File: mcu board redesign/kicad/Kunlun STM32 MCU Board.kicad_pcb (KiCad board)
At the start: 2 copper layers, 40 x 40 mm, 33 parts, among them J1 0532610671, J2 10129383-908001ALF, J3 USB4105-GF-A, J4 5002, J5 5002, J6 5002, J7 5002, J8 5001, J9 5001, SW1 KMR231NG ULC LFS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

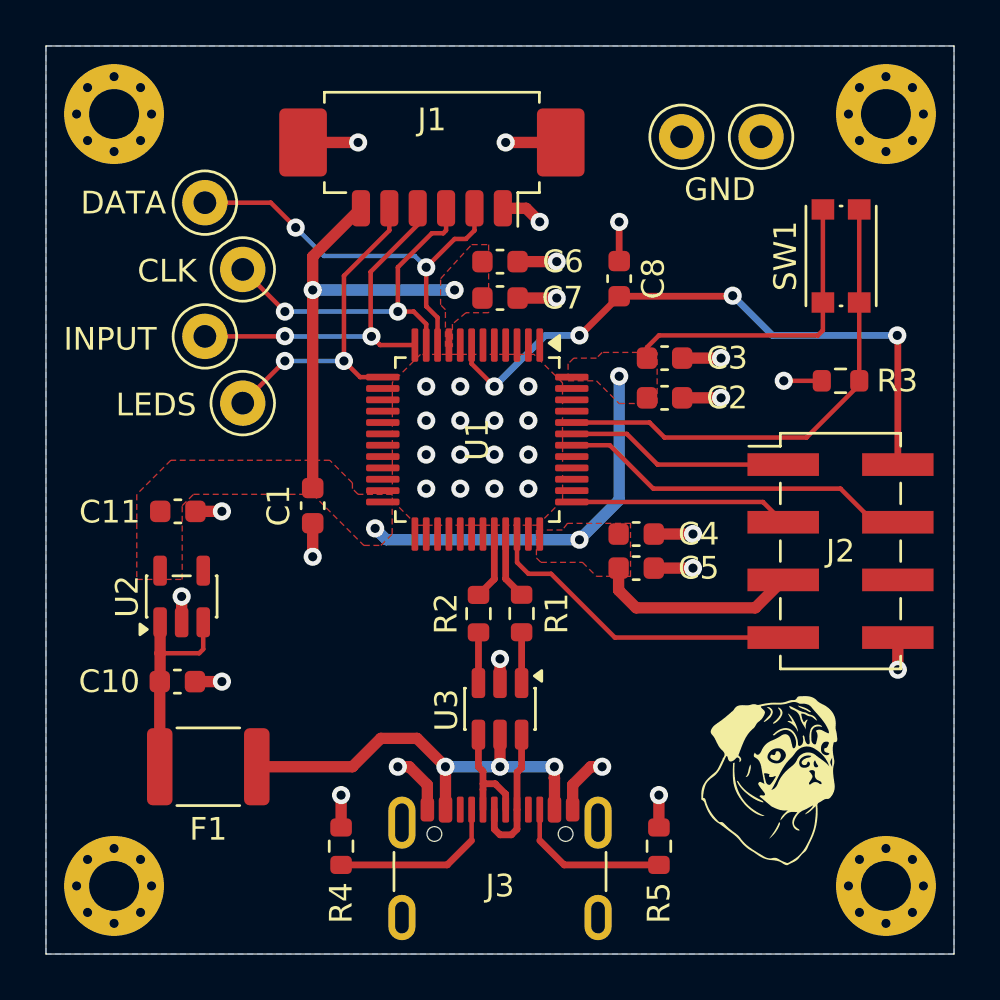
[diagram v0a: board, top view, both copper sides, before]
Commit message: Lots of updates
Add ESD protection R6/C9
Layout changes for bypass caps
Layout changes to pass all JLC DFM checks
Fill out J2 and optimize routing
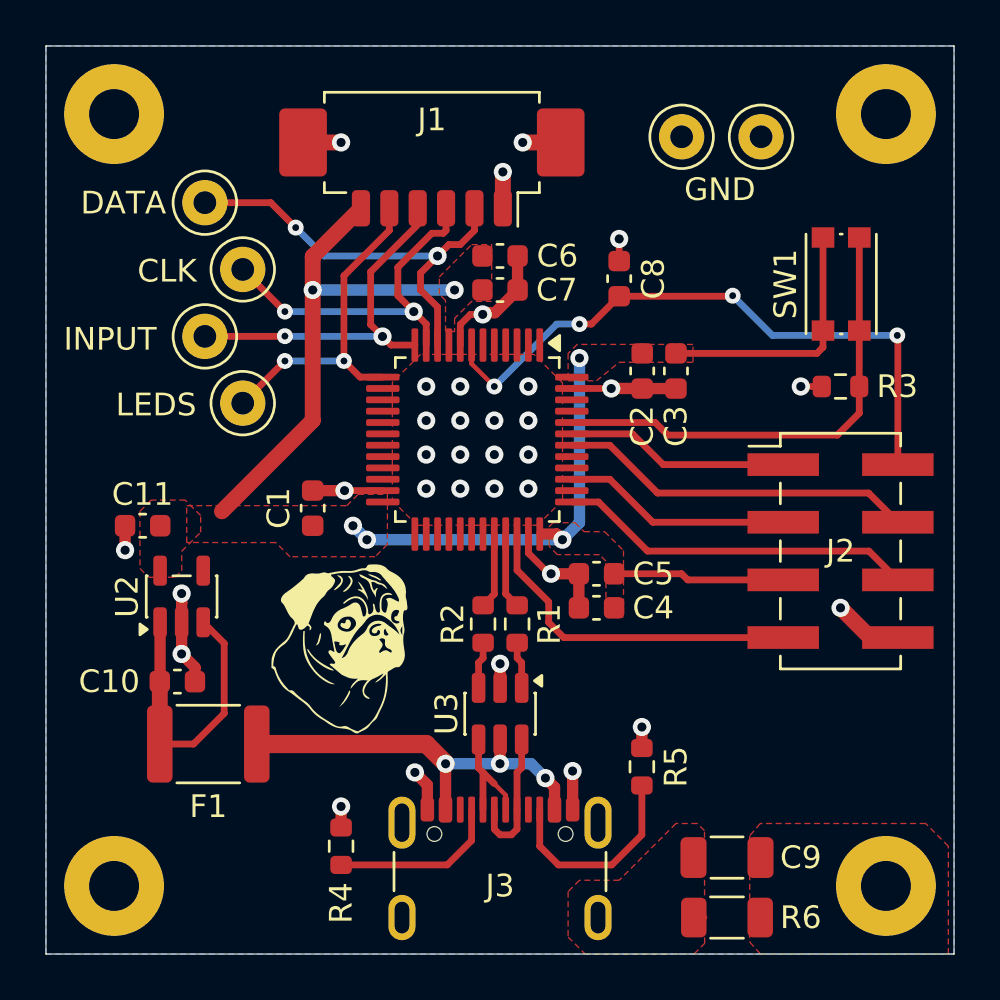
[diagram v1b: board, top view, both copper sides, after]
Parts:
- added C9: 1nF, Capacitor_SMD:C_1206_3216Metric, F.Cu at (158.2, 120.5)
- added R6: 1M, Resistor_SMD:R_1206_3216Metric, F.Cu at (158.2, 123.1)
- H1, H2, H3, H4: footprint MountingHole:MountingHole_2.2mm_M2_Pad_Via -> MountingHole:MountingHole_2.2mm_M2_Pad
- moved H1 48.1 mm to (165.2, 121.8)
- moved H2 48.1 mm to (131.2, 121.8)
- moved H3 34.0 mm to (131.2, 87.8)
- moved H4 34.0 mm to (165.2, 87.8)
- moved C4 3.69 mm to (152.5, 109.5), turned to 180 degrees
- moved R5 3.58 mm to (154.5, 116.5)
- moved C5 1.77 mm to (152.5, 108.0), turned to 180 degrees
- moved C11 1.67 mm to (132.5, 105.9), turned to 180 degrees
- moved C2 1.54 mm to (154.5, 99.1), turned to -90 degrees
- moved SW1 1.24 mm to (163.3, 95.2)
- moved F1 1.00 mm to (135.4, 115.5)
- moved C3 0.76 mm to (156.0, 99.1), turned to -90 degrees
- moved R1 0.50 mm to (149.0, 110.2)
- moved R2 0.50 mm to (147.5, 110.2)
- moved C7 0.35 mm to (148.2, 95.5)
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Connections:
- H1 pad 1: GND -> Net-(C9-Pad1)
- H2 pad 1: GND -> unconnected-(H2-Pad1)
- H3 pad 1: GND -> unconnected-(H3-Pad1)
- H4 pad 1: GND -> unconnected-(H4-Pad1)
- J2 pad 3: /SWCLK -> /DEBUG_GPIO
- J2 pad 6: unconnected-(J2-Pin_6-Pad6) -> /SWCLK
- R1 pad 1: Net-(R1-Pad1) -> /USB_D+
- R1 pad 2: /USB_D+ -> Net-(U1-PA12)
- R2 pad 1: Net-(R2-Pad1) -> /USB_D-
- R2 pad 2: /USB_D- -> Net-(U1-PA11)
- U1 pad 32: /USB_D- -> Net-(U1-PA11)
- U1 pad 33: /USB_D+ -> Net-(U1-PA12)
- U1 pad 39: unconnected-(U1-PB3-Pad39) -> /DEBUG_GPIO
- U3 pad 1: Net-(R1-Pad1) -> /USB_D+
- U3 pad 3: Net-(R2-Pad1) -> /USB_D-
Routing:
- net /DEBUG_GPIO: track 0.00 -> 10.1 mm
- net /SWCLK: track 9.68 -> 17.0 mm
- net +5V: track 9.53 -> 13.2 mm
- net GND: track 36.2 -> 39.6 mm, vias 36 -> 33
- net Net-(U1-PA12): track 0.00 -> 3.35 mm
- net Net-(U1-PA11): track 0.00 -> 3.34 mm
- net Net-(R1-Pad1): track 2.24 -> 0.00 mm
- net Net-(R2-Pad1): track 2.24 -> 0.00 mm
- net Net-(J3-CC2): track 7.06 -> 9.18 mm
- net VBUS: track 19.3 -> 17.9 mm
- net unconnected-(J2-Pin_6-Pad6): track 1.25 -> 0.00 mm
- net /USART1_TX: track 15.8 -> 16.8 mm
- net /USB_D-: track 2.97 -> 2.07 mm
- net /USB_D+: track 2.97 -> 2.07 mm
- net /SWDIO: track 14.3 -> 15.1 mm
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- added copper zone on F.Cu, net Net-(C9-Pad1)
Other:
- board text added: "J2 1-UART1_RX 2-NRST 3-PB3 4-UART1_TX 5-VDD (3.3V) 6-SWCLK 7-SWDIO 8-GND"
- board text removed: "J2 1-UART1_RX 2-NRST 3-SWCLK 4-UART1_TX 5-VDD (3.3V) 6- 7-SWDIO 8-GND"

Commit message: Mostly layout updates
Add VBUS decoupling cap.
Rearrange traces for less ground plane chops and fewer vias.
Move some components around for trace optimization (boot switch, etc)
Tweak the decoupling caps
Remove pads from 3 mounting holes to avoid potential chassis ground loops
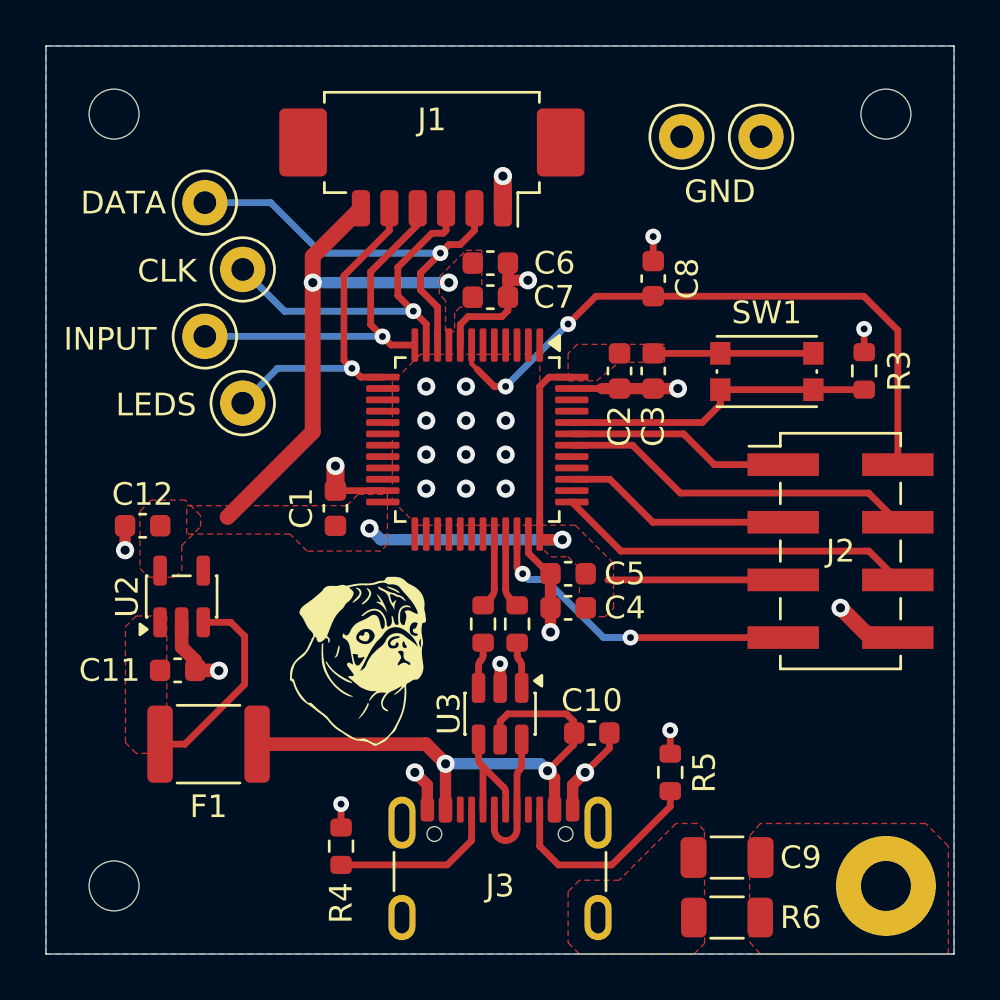
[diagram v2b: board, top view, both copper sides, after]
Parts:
- removed H2, H3, H4: MountingHole_Pad, MountingHole:MountingHole_2.2mm_M2_Pad
- added C10: 1uF, Capacitor_SMD:C_0603_1608Metric, F.Cu at (152.3, 115.0)
- added REF**: MountingHole_2.2mm_M2, MountingHole:MountingHole_2.2mm_M2, F.Cu at (131.2, 121.8)
- added REF**: MountingHole_2.2mm_M2, MountingHole:MountingHole_2.2mm_M2, F.Cu at (165.2, 87.8)
- added REF**: MountingHole_2.2mm_M2, MountingHole:MountingHole_2.2mm_M2, F.Cu at (131.2, 87.8)
- C8: value 0.1uF -> 100nF
- moved SW1 5.06 mm to (160.0, 99.1), turned to 0 degrees
- moved C8 1.50 mm to (155.0, 95.0)
- moved R5 1.27 mm to (155.8, 116.8)
- moved C4 1.25 mm to (151.2, 109.5)
- moved C5 1.25 mm to (151.2, 108.0)
- moved R3 1.25 mm to (164.3, 99.1), turned to 90 degrees
- moved C1 1.00 mm to (141.0, 105.1)
- moved C2 1.00 mm to (153.5, 99.1)
- moved C3 1.00 mm to (155.0, 99.1)
- moved C6 0.53 mm to (147.8, 94.3)
- moved C7 0.53 mm to (147.8, 95.8)
- moved C11 0.50 mm to (134.1, 112.3)
- renumbered C10 to C11, C11 to C12
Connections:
- J1 pad MP: GND -> unconnected-(J1-MountPin-PadMP)_1
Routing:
- net /BOOT0: track 21.0 -> 13.9 mm
- net VBUS: track 17.9 -> 24.0 mm, vias 3 -> 2
- net +3.3V: track 60.0 -> 54.4 mm, vias 6 -> 4
- net +5V: track 13.2 -> 9.02 mm
- net GND: track 39.6 -> 37.4 mm, vias 33 -> 26
- net /SWCLK: track 17.0 -> 15.8 mm
- net /USART1_TX: track 16.8 -> 15.8 mm
- net /SWDIO: track 15.1 -> 14.5 mm, vias 0 -> 2
- net Net-(C9-Pad1): track 0.53 -> 0.00 mm
- net /WS2812_LED_DATA: track 14.8 -> 15.0 mm, vias 2 -> 1
- net /MATRIX_DATA/L_INPUT: track 18.8 -> 18.9 mm, vias 2 -> 1
- net /MATRIX_R_INPUT: track 16.2 -> 16.1 mm, vias 2 -> 1
- net /NRST: vias 4 -> 2
- net /MATRIX_CLOCK: vias 2 -> 1
- added copper zone on F.Cu, net +5V
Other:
- board text added: "J2 1-UART1_RX 2-NRST 3-PB3 4-UART1_TX 5-VDD 6-SWCLK 7-SWDIO 8-GND"
- board text added: "project 802 Kunlun STM32 MCU Board"
- board text added: "r1"
- board text removed: "J2 1-UART1_RX 2-NRST 3-PB3 4-UART1_TX 5-VDD (3.3V) 6-SWCLK 7-SWDIO 8-GND"
- board text removed: "project 802 Kunlun MCU Board"

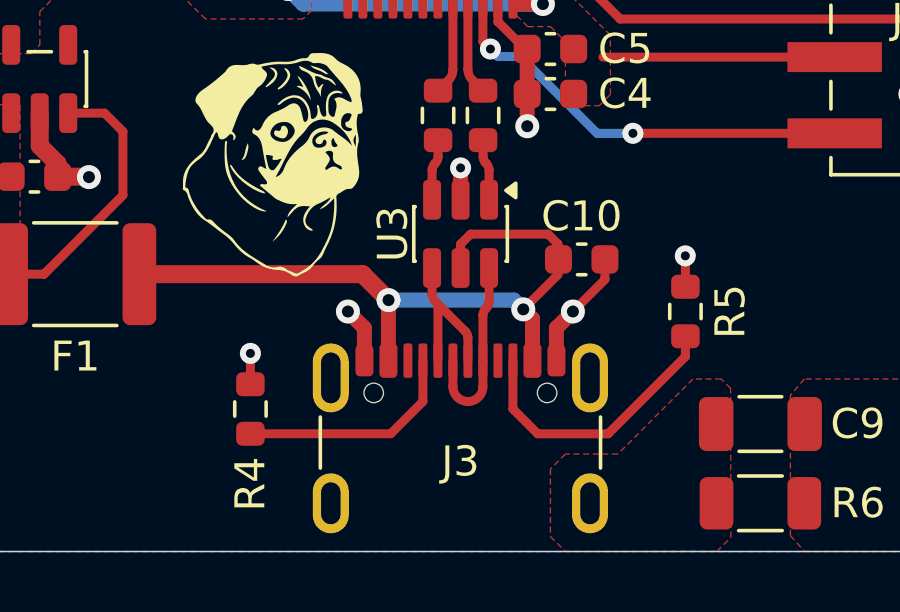
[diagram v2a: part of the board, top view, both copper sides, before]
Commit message: Make D- pretty at the connector
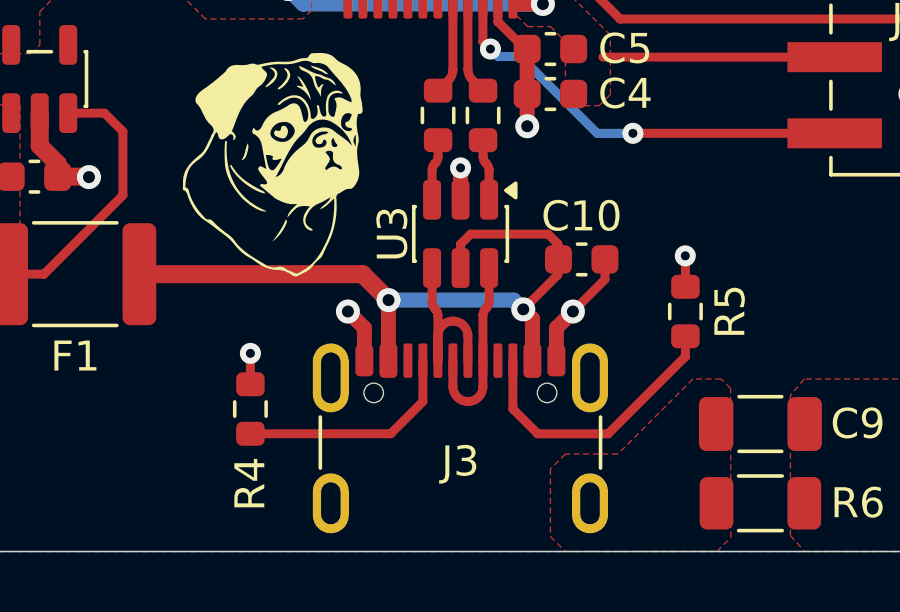
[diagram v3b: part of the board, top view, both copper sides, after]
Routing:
- net /D-: track 5.44 -> 6.39 mm
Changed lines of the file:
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@@
 	)
 	(segment
-		(start 147.5 118.387601)
-		(end 147.5 116.5)
+		(start 148.5 118.4312)
+		(end 148.5 117.568801)
 		(width 0.3)
 		(layer "F.Cu")
@@
 	)
 	(segment
-		(start 148.412132 117.412132)
-		(end 147.5 116.5)
+		(start 147.5 118.387601)
+		(end 147.5 116.874264)
 		(width 0.3)
 		(layer "F.Cu")
@@
 	)
 	(segment
-		(start 148.5 118.387601)
-		(end 148.5 117.624264)
-		(width 0.3)
-		(layer "F.Cu")
-		(net "/D-")
-	)
-	(segment
-		(start 147.305244 116.18098)
+		(start 147.305244 116.43098)
 		(end 147.305244 115.30067)
 		(width 0.3)
@@
 	)
 	(segment
-		(start 147.5 116.5)
-		(end 147.393112 116.393112)
+		(start 147.5 117.568801)
+		(end 147.5 118.4312)
+		(width 0.3)
+		(layer "F.Cu")
+		(net "/D-")
+	)
+	(segment
+		(start 147.412132 116.662132)
+		(end 147.393112 116.643112)
 		(width 0.3)
 		(layer "F.Cu")
@@
 	)
 	(arc
-		(start 147.393112 116.393112)
-		(mid 147.32808 116.295785)
-		(end 147.305244 116.18098)
+		(start 148 117.068801)
+		(mid 147.646447 117.215248)
+		(end 147.5 117.568801)
 		(width 0.3)
 		(layer "F.Cu")
@@
 	)
 	(arc
-		(start 148.5 117.624264)
-		(mid 148.477164 117.509459)
-		(end 148.412132 117.412132)
+		(start 147.5 116.874264)
+		(mid 147.477164 116.759459)
+		(end 147.412132 116.662132)
 		(width 0.3)
 		(layer "F.Cu")
+		(net "/D-")
+	)
+	(arc
+		(start 147.393112 116.643112)
+		(mid 147.32808 116.545785)
+		(end 147.305244 116.43098)
+		(width 0.3)
+		(layer "F.Cu")
+		(net "/D-")
+	)
+	(arc
+		(start 148.5 117.568801)
+		(mid 148.353553 117.215248)
+		(end 148 117.068801)
+		(width 0.3)
+		(layer "F.Cu")
